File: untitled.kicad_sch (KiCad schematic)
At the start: 26 parts, among them SW1 SW_Push, SW3 SW_Push, U1 ESP32-S3, U2 W25Q16JVSS, U3 ME6231A33PG, Y1 Crystal_GND24

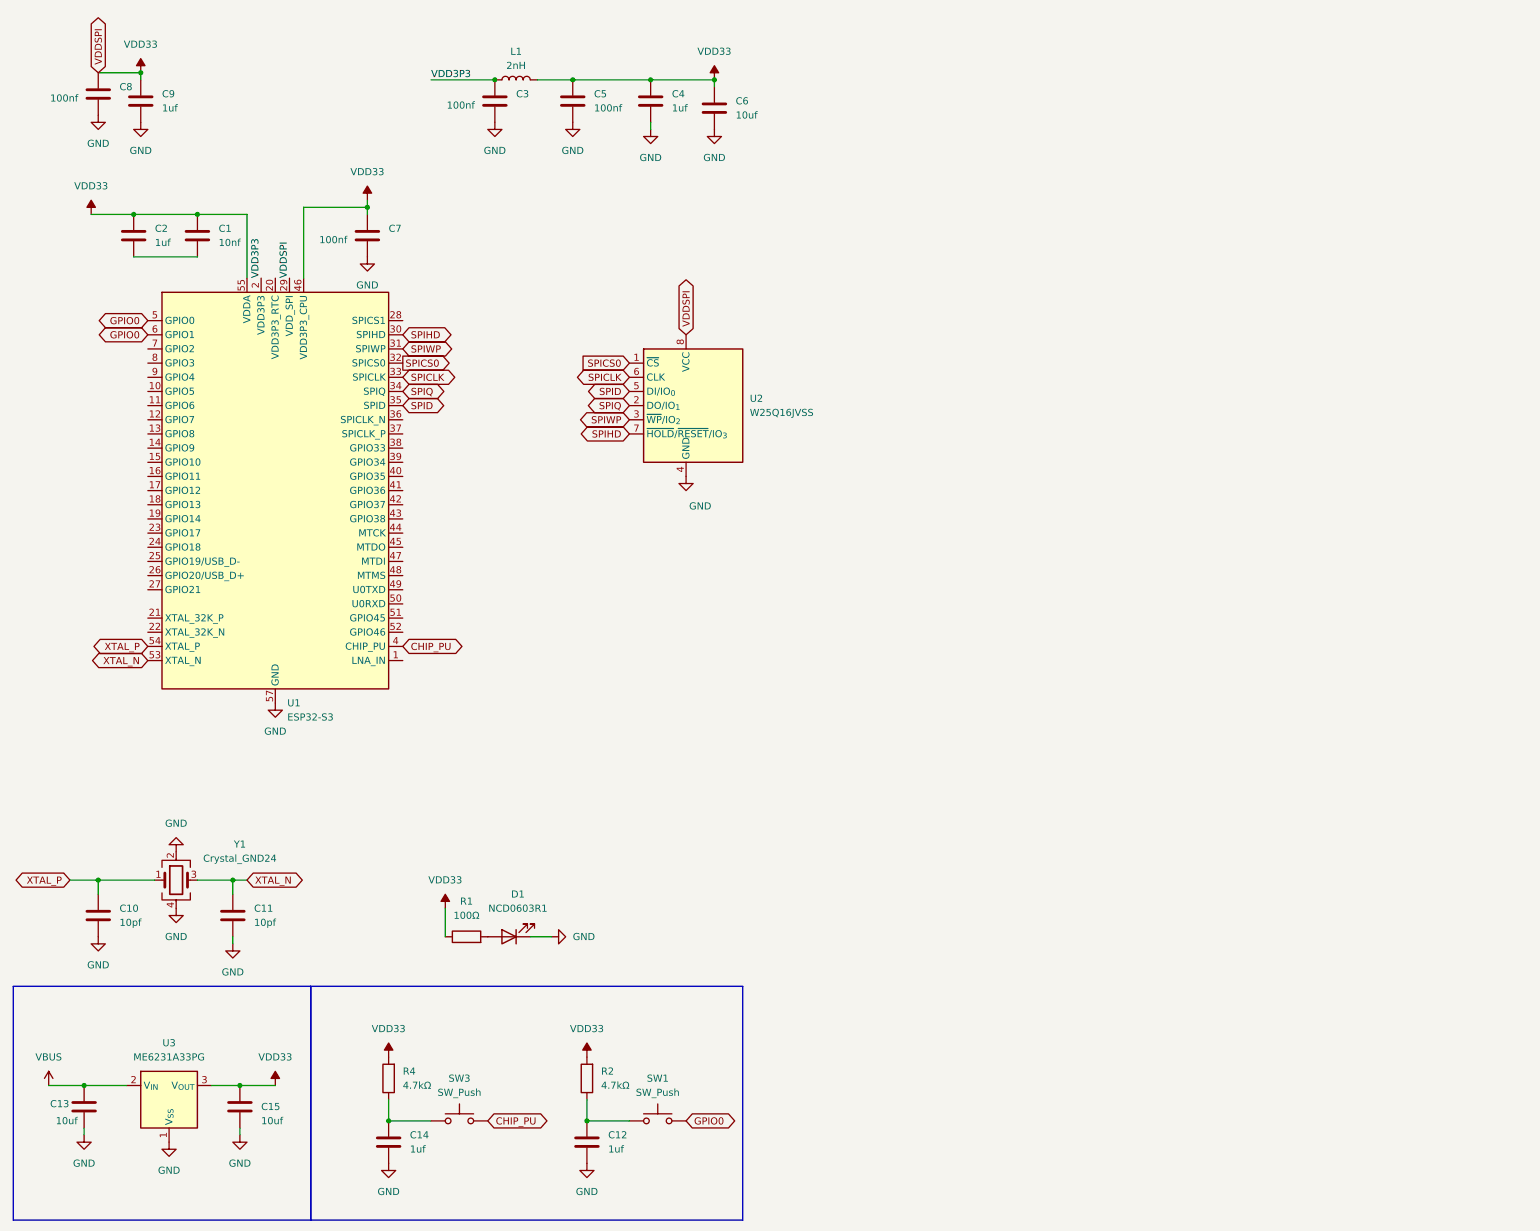
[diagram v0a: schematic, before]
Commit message: 添加引脚标注
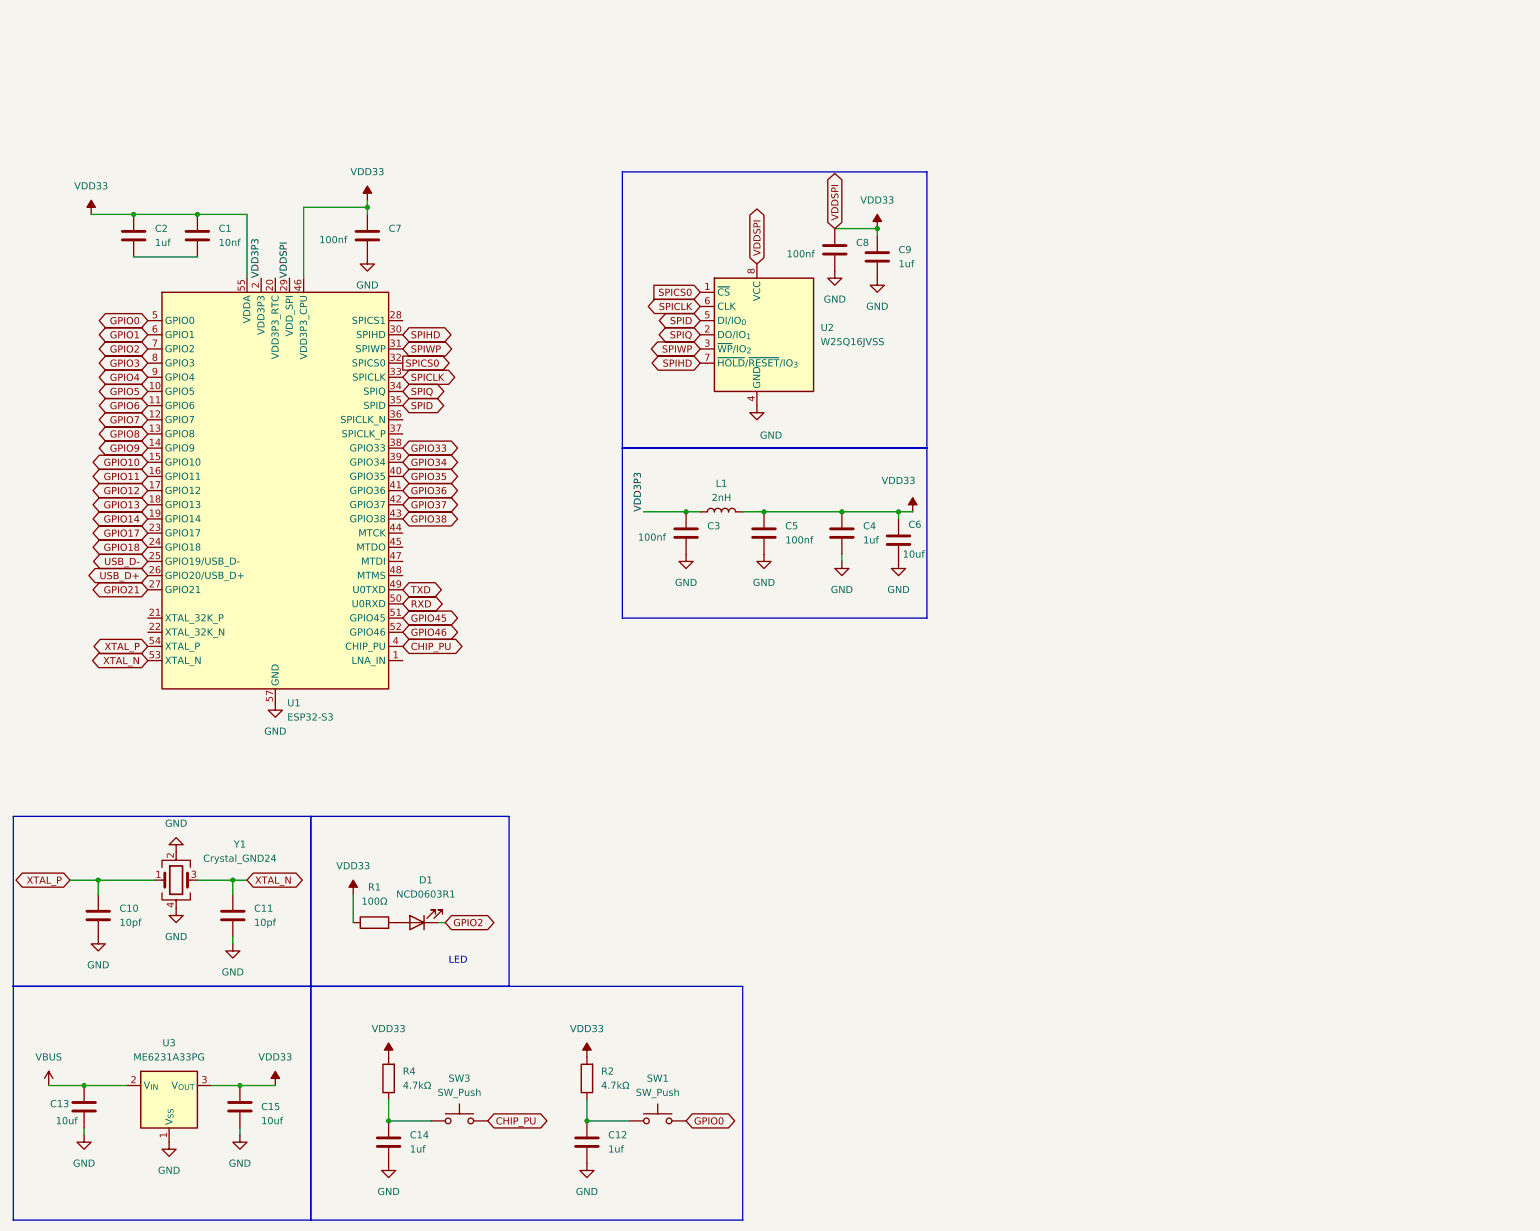
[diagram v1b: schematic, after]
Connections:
- net GND: no longer D1.1 (K)
- net GPIO0: no longer U1.6 (GPIO1)
- net GPIO5: now reaches U1.10 (GPIO5)
- net GPIO6: now reaches U1.11 (GPIO6)
- net GPIO7: now reaches U1.12 (GPIO7)
- net GPIO8: now reaches U1.13 (GPIO8)
- net GPIO9: now reaches U1.14 (GPIO9)
- net GPIO10: now reaches U1.15 (GPIO10)
- net GPIO11: now reaches U1.16 (GPIO11)
- net GPIO12: now reaches U1.17 (GPIO12)
- net GPIO13: now reaches U1.18 (GPIO13)
- net GPIO14: now reaches U1.19 (GPIO14)
- net GPIO17: now reaches U1.23 (GPIO17)
- net GPIO18: now reaches U1.24 (GPIO18)
- net USB_D-: now reaches U1.25 (GPIO19/USB_D-)
- net USB_D+: now reaches U1.26 (GPIO20/USB_D+)
- net GPIO21: now reaches U1.27 (GPIO21)
- net GPIO33: now reaches U1.38 (GPIO33)
- net GPIO34: now reaches U1.39 (GPIO34)
- net GPIO35: now reaches U1.40 (GPIO35)
- net GPIO36: now reaches U1.41 (GPIO36)
- net GPIO37: now reaches U1.42 (GPIO37)
- net GPIO38: now reaches U1.43 (GPIO38)
- net TXD: now reaches U1.49 (U0TXD)
- net RXD: now reaches U1.50 (U0RXD)
- net GPIO45: now reaches U1.51 (GPIO45)
- net GPIO46: now reaches U1.52 (GPIO46)
- net GPIO2: now reaches U1.7 (GPIO2)
- net GPIO2: now also D1.1 (K)
- net GPIO3: now reaches U1.8 (GPIO3)
- net GPIO4: now reaches U1.9 (GPIO4)
- new net GPIO1: U1.6 (GPIO1)
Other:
- note added: "LED"
- moved on the sheet: C3, C4, C5, C6, C8, C9, D1, L1, R1, U2

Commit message: 🚀初步完善原理图
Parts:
- added AE2: Antenna_Shield, RF_Antenna:Texas_SWRA117D_2.4GHz_Left, symbol Device:Antenna_Shield
- added C16: 100nf, Capacitor_SMD:C_0402_1005Metric, symbol Device:C
- added C17: 1uf, Capacitor_SMD:C_0402_1005Metric, symbol Device:C
- added C18, C19: 15pf, Capacitor_SMD:C_0402_1005Metric, symbol Device:C
- added C20: 4.7PF, Capacitor_SMD:C_0402_1005Metric, symbol Device:C
- added C21: 2.4pf, Capacitor_SMD:C_0402_1005Metric, symbol Device:C
- added D2: NCD0603R1, LED_SMD:LED_0603_1608Metric, symbol Device:LED
- added J1, J2: USB1, Connector_USB:USB_C_Receptacle_G-Switch_GT-USB-7010ASV, symbol Connector:USB_C_Receptacle_USB2.0_14P
- added L2: 2.4nh, Inductor_SMD:L_0402_1005Metric, symbol Device:L
- added R3, R5, R6, R7: 5.1K, Resistor_SMD:R_0402_1005Metric, symbol Device:R
- added R8: 100Ω, Resistor_SMD:R_0402_1005Metric, symbol Device:R
- added U4: CH343P, Package_DFN_QFN:WCH_QFN-16-1EP_3x3mm_P0.5mm_EP1.8x1.8mm, symbol Interface_USB:CH343P
- added Y2: Crystal, SmartLock:Crystal_SMD_ECS_CSM3X-2Pin_7.5x3.1mm, symbol Device:Crystal
- D1: footprint (none) -> LED_SMD:LED_0603_1608Metric
- SW1, SW3: footprint (none) -> SmartLock:SW-SMD_L3.9-W3.0-P4.45
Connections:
- net CHIP_PU: now also U4.13 (~{RTS})
- net GND: now also AE2.2 (Shield), C16.1, C17.1, C18.1, C19.2, C21.1, D2.1 (K), J1.A1 (GND), J1.A12 (GND), J1.B1 (GND), J1.B12 (GND), J1.S1 (SHIELD), J2.A1 (GND), J2.A12 (GND), J2.B1 (GND), J2.B12 (GND), J2.S1 (SHIELD), L2.2, R3.1, R5.1, R6.1, R7.1, U4.17 (GND_EPAD), U4.2 (GND)
- net GPIO0: now also U4.12 (~{DTR})
- net RXD: now also U4.4 (TXD)
- net TXD: now also U4.5 (RXD)
- net USB_D+: now also J2.A6 (D+), J2.B6 (D+)
- net USB_D-: now also J2.A7 (D-), J2.B7 (D-)
- net VBUS: now also J1.A4 (VBUS), J1.A9 (VBUS), J1.B4 (VBUS), J1.B9 (VBUS), J2.A4 (VBUS), J2.A9 (VBUS), J2.B4 (VBUS), J2.B9 (VBUS), U4.3 (VDD5), U4.9 (VBUS)
- net VDD33: now also C17.2, R8.1, U4.1 (VIO)
- net LNA_IN: now reaches U1.1 (LNA_IN)
- net LNA_IN: now also C20.1, L2.1
- net RTC_P: now reaches U1.21 (XTAL_32K_P)
- net RTC_P: now also C18.2, Y2.2
- net RTC_N: now reaches U1.22 (XTAL_32K_N)
- net RTC_N: now also C19.1, Y2.1
- net GPIO48: now reaches U1.36 (SPICLK_N)
- net GPIO47: now reaches U1.37 (SPICLK_P)
- net GPIO39: now reaches U1.44 (MTCK)
- net GPIO40: now reaches U1.45 (MTDO)
- net GPIO41: now reaches U1.47 (MTDI)
- net GPIO42: now reaches U1.48 (MTMS)
- new net: J2.A5 (CC1), R6.2
- new net: AE2.1 (A), C20.2, C21.2
- new net: D2.2 (A), R8.2
- new net: C16.2, U4.6 (V3_{OUT})
- new net: J2.B5 (CC2), R7.2
- new net: J1.A5 (CC1), R3.2
- new net: J1.B5 (CC2), R5.2
- new net U+: J1.A6 (D+), J1.B6 (D+), U4.7 (UD+)
- new net U-: J1.A7 (D-), J1.B7 (D-), U4.8 (UD-)
- no-connect marks 0 -> 5
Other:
- note added: "BOOT"
- note added: "EN"
- note added: "FLASH"
- note added: "LDO"
- note added: "OTG"
- note added: "RTC"
- note added: "TYPEC--UART"
- note added: "UART一键下载"
- moved on the sheet: C3, C4, C5, C6, C8, C9, L1, U2
